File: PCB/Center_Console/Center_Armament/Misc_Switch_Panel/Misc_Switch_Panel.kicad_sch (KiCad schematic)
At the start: 0 parts

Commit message: Misc Switch Panel schematic WIP + gitignore cleanup
- Misc_Switch_Panel: schematic and PCB in-progress (MCP23017, 8-pin JST-XH harness)
- .gitignore: exclude KiCad Fabrication Toolkit outputs (production/, fabrication-toolkit-options.json) and .claude/worktrees/
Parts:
- added J1: Conn_02x04_Top_Bottom, Connector_Molex:Molex_Mini-Fit_Jr_5566-08A_2x04_P4.20mm_Vertical, symbol Connector_Generic:Conn_02x04_Top_Bottom
- added U1: MCP23017x-x-SO, Package_SO:SOIC-28W_7.5x17.9mm_P1.27mm, symbol Interface_Expansion:MCP23017x-x-SO
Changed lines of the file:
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@@
 	(generator_version "10.0")
 	(paper "A4")
+	(symbol
+		(lib_id "Interface_Expansion:MCP23017x-x-SO")
+		(at 68.58 62.23 0)
+		(unit 1)
+		(body_style 1)
+		(exclude_from_sim no)
+		(in_bom yes)
+		(on_board yes)
+		(in_pos_files yes)
+		(dnp no)
+		(fields_autoplaced yes)
+		(property "Reference" "U1"
+			(at 70.7233 34.29 0)
+			(show_name no)
+			(do_not_autoplace no)
+			(effects
+				(font
+					(size 1.27 1.27)
+				)
+				(justify left)
+			)
+		)
+		(property "Value" "MCP23017x-x-SO"
+			(at 70.7233 36.83 0)
+			(show_name no)
+			(do_not_autoplace no)
+			(effects
+				(font
+					(size 1.27 1.27)
+				)
+				(justify left)
+			)
+		)
+		(property "Footprint" "Package_SO:SOIC-28W_7.5x17.9mm_P1.27mm"
+			(at 73.66 87.63 0)
+			(hide yes)
+			(show_name no)
+			(do_not_autoplace no)
+			(effects
+				(font
+					(size 1.27 1.27)
+				)
+				(justify left)
+			)
+		)
+		(property "Datasheet" "https://ww1.microchip.com/downloads/aemDocuments/documents/APID/ProductDocuments/DataSheets/MCP23017-Data-Sheet-DS20001952.pdf"
+			(at 73.66 90.17 0)
+			(hide yes)
+			(show_name no)
+			(do_not_autoplace no)
+			(effects
+				(font
+					(size 1.27 1.27)
+				)
+				(justify left)
+			)
+		)
+		(property "Description" "16-bit I/O expander, I2C, interrupts, w pull-ups, GPA7/GPB7 output only (https://microchip.my.site.com/s/article/GPA7---GPB7-Cannot-Be-Used-as-Inputs-In-MCP23017),  SOIC-28"
+			(at 68.58 62.23 0)
+			(hide yes)
+			(show_name no)
+			(do_not_autoplace no)
+			(effects
+				(font
+					(size 1.27 1.27)
+				)
+			)
+		)
+		(pin "6"
+		)
+		(pin "3"
+		)
+		(pin "1"
+		)
+		(pin "7"
+		)
+		(pin "8"
+		)
+		(pin "2"
+		)
+		(pin "4"
+		)
+		(pin "5"
+		)
+		(pin "9"
+		)
+		(pin "28"
+		)
+		(pin "23"
+		)
+		(pin "26"
+		)
+		(pin "24"
+		)
+		(pin "27"
+		)
+		(pin "25"
+		)
+		(pin "12"
+		)
+		(pin "11"
+		)
+		(pin "10"
+		)
+		(pin "16"
+		)
+		(pin "15"
+		)
+		(pin "17"
+		)
+		(pin "14"
+		)
+		(pin "13"
+		)
+		(pin "22"
+		)
+		(pin "18"
+		)
+		(pin "21"
+		)
+		(pin "20"
+		)
+		(pin "19"
+		)
+		(instances
+			(project "Misc_Switch_Panel"
+				(path "/e216e2c6-0c29-44a6-a74b-9257e68cb7df"
+					(reference "U1")
+					(unit 1)
+				)
+			)
+		)
+	)
+	(symbol
+		(lib_id "Connector_Generic:Conn_02x04_Top_Bottom")
+		(at 140.97 43.18 0)
+		(unit 1)
+		(body_style 1)
+		(exclude_from_sim no)
+		(in_bom yes)
+		(on_board yes)
+		(in_pos_files yes)
+		(dnp no)
+		(fields_autoplaced yes)
+		(property "Reference" "J1"
+			(at 142.24 34.29 0)
+			(show_name no)
+			(do_not_autoplace no)
+			(effects
+				(font
+					(size 1.27 1.27)
+				)
+			)
+		)
+		(property "Value" "Conn_02x04_Top_Bottom"
+			(at 142.24 36.83 0)
+			(show_name no)
+			(do_not_autoplace no)
+			(effects
+				(font
+					(size 1.27 1.27)
+				)
+			)
+		)
+		(property "Footprint" "Connector_Molex:Molex_Mini-Fit_Jr_5566-08A_2x04_P4.20mm_Vertical"
+			(at 140.97 43.18 0)
+			(hide yes)
+			(show_name no)
+			(do_not_autoplace no)
+			(effects
+				(font
+					(size 1.27 1.27)
+				)
+			)
+		)
+		(property "Datasheet" ""
+			(at 140.97 43.18 0)
+			(hide yes)
+			(show_name no)
+			(do_not_autoplace no)
+			(effects
+				(font
+					(size 1.27 1.27)
+				)
+			)
+		)
+		(property "Description" "Generic connector, double row, 02x04, top/bottom pin numbering scheme (row 1: 1...pins_per_row, row2: pins_per_row+1 ... num_pins), script generated (kicad-library-utils/schlib/autogen/connector/)"
+			(at 140.97 43.18 0)
+			(hide yes)
+			(show_name no)
+			(do_not_autoplace no)
+			(effects
+				(font
+					(size 1.27 1.27)
+				)
+			)
+		)
+		(pin "1"
+		)
+		(pin "3"
+		)
+		(pin "2"
+		)
+		(pin "4"
+		)
+		(pin "5"
+		)
+		(pin "6"
+		)
+		(pin "7"
+		)
+		(pin "8"
+		)
+		(instances
+			(project "Misc_Switch_Panel"
+				(path "/e216e2c6-0c29-44a6-a74b-9257e68cb7df"
+					(reference "J1")
+					(unit 1)
+				)
+			)
+		)
+	)
 	(sheet_instances
 		(path "/"

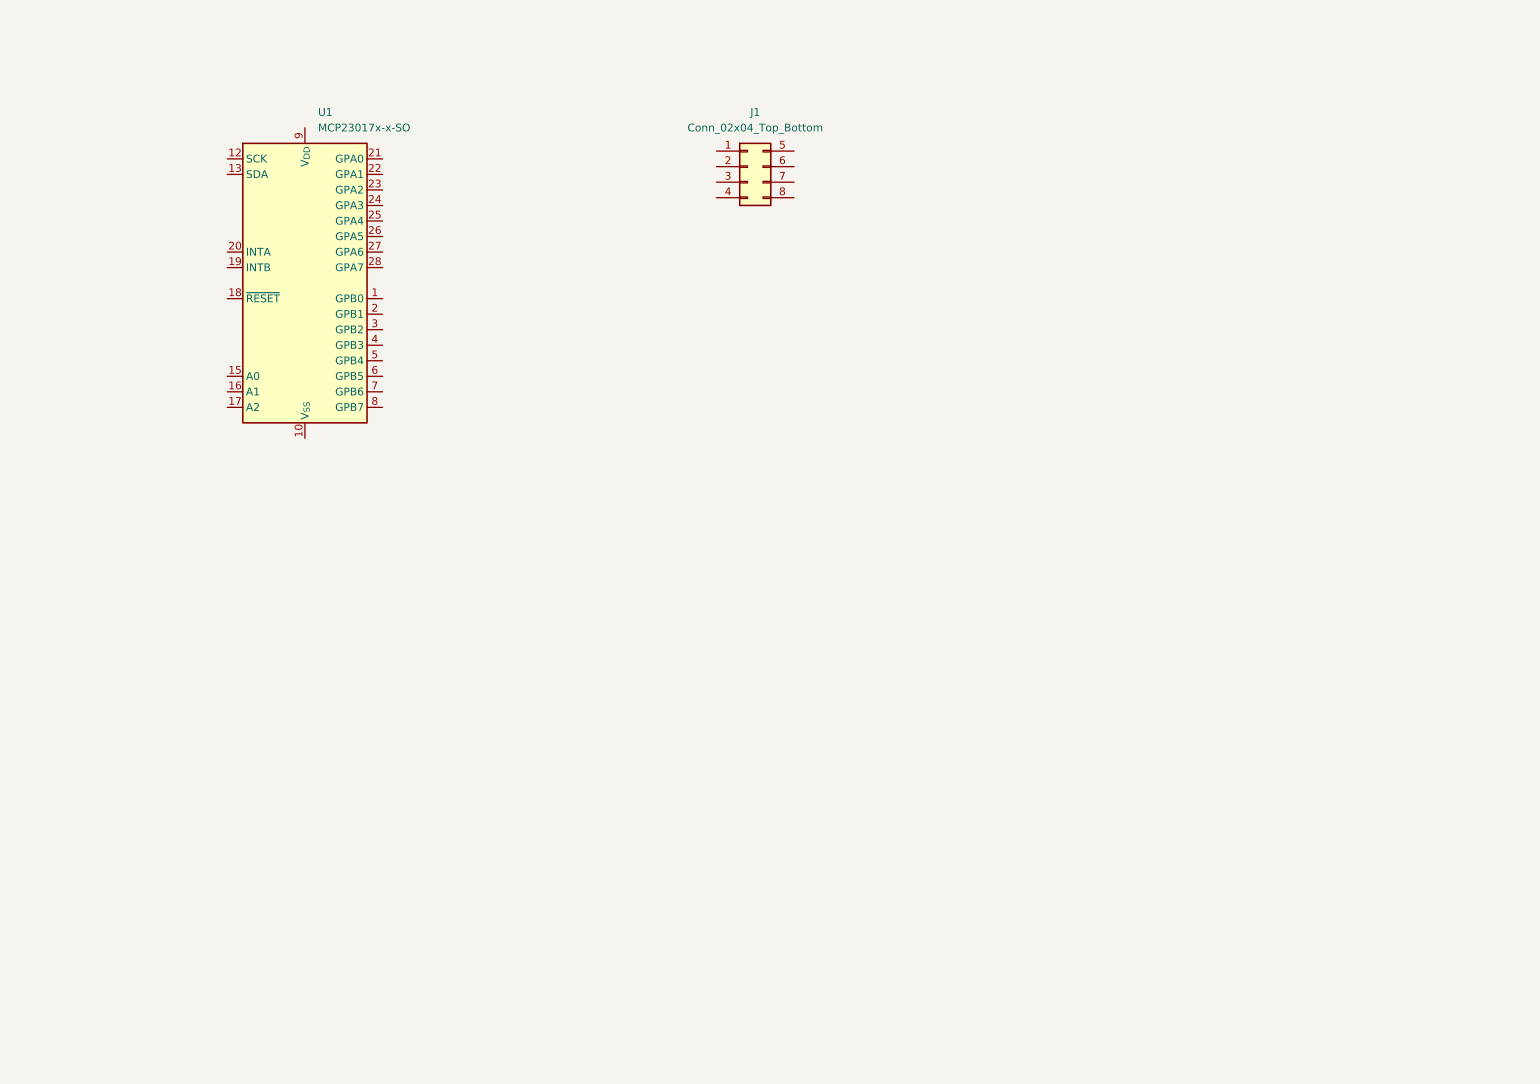
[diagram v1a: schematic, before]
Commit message: Complete Misc Switch Panel schematic and establish shared PCB infrastructure
Misc Switch Panel schematic (3 sheets, 0 ERC violations):
- Controls sheet: MCP23017 @ 0x22, 8-pin JST-XH harness (J1), address/reset
  resistors, I2C series (33Ω) and interrupt protection (100Ω) resistors
- Switches sheet: J2/J3 8-pin JST-XH connectors, all panel-mounted switch and
  pot symbols (exclude_from_board)
- Backlighting sheet: 3× 5-LED series strings, 120Ω per string, hierarchical
  labels +12V_BACKLIGHT / BACKLIGHT_SW_RETURN
- LED zone switching: IRLML2502 N-ch low-side MOSFET, gate driven directly by
  STM32 3.3V PWM; LED power on separate 2-pin Mini-Fit Jr (J4), not on signal
  harness — eliminates NPN+zener gate driver complexity

Shared KiCad project infrastructure:
- /new-kicad-project skill: scaffolds directory, lib tables, .kicad_pro, and
  minimal root .kicad_sch in one step; tailored next-steps for mcu vs breakout
- PCB/Libraries/project-template/template.kicad_pro: JLCPCB design rules,
  predefined track widths (0.2/0.3/0.5/1.0mm), via sizes (0.3/0.6, 0.4/0.8mm),
  4 net classes (Default, LED_Trunk, LED_String, CAN), silkscreen defaults
- PCB/Libraries/design-rules/jlcpcb-standard.kicad_dru: custom DRC rules for
  copper-to-edge, silkscreen width, hole-to-hole, CAN diff pair
- PCB/Libraries/sheets/README.md: shared hierarchical sheet template library
  (placeholder; templates added as standard blocks are completed)
- Misc_Switch_Panel.kicad_pro patched with all of the above

PCB design rules documented (Docs/claude/pcb-design-rules.md):
- JLCPCB standard 2-layer constraints; min trace/clearance bumped to 0.2mm
  (floor matches Default class — all DRC violations are meaningful)
- Net class table with sizing rationale; power classes deferred pending actuator
  board architecture; 500mA per-board limit for logic+LED boards established
- Actuator board checklist placeholder (solenoids, servos, large steppers)
- JLCPCB cost-optimised ordering settings from bench-verified s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
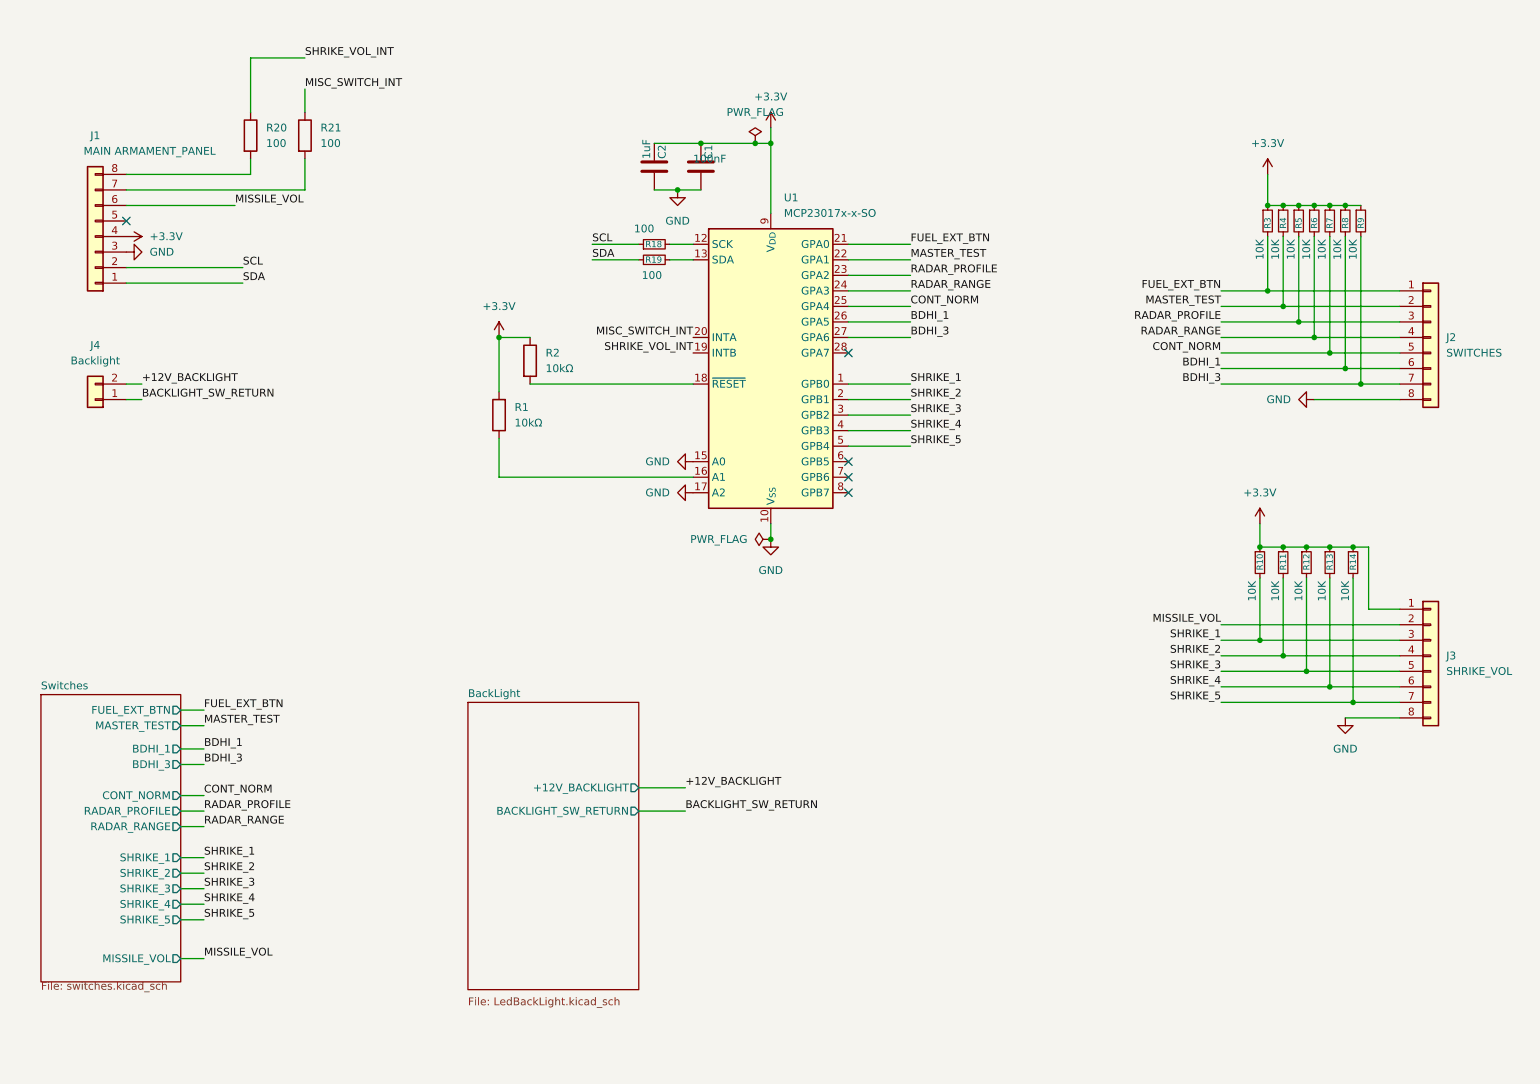
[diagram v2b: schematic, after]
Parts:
- removed J1: Conn_02x04_Top_Bottom, Connector_Molex:Molex_Mini-Fit_Jr_5566-08A_2x04_P4.20mm_Vertical, symbol Connector_Generic:Conn_02x04_Top_Bottom
- added C1: 100nF, Capacitor_SMD:C_0805_2012Metric, symbol Device:C
- added C2: 1uF, Capacitor_SMD:C_0805_2012Metric, symbol Device:C
- added J1: MAIN ARMAMENT_PANEL, Connector_JST:JST_XH_B8B-XH-A_1x08_P2.50mm_Vertical, symbol Connector_Generic:Conn_01x08
- added J2: SWITCHES, Connector_JST:JST_XH_B8B-XH-A_1x08_P2.50mm_Vertical, symbol Connector_Generic:Conn_01x08
- added J3: SHRIKE_VOL, Connector_JST:JST_XH_B8B-XH-A_1x08_P2.50mm_Vertical, symbol Connector_Generic:Conn_01x08
- added J4: Backlight, Connector_Molex:Molex_Mini-Fit_Jr_5566-02A_2x01_P4.20mm_Vertical, symbol Connector_Generic:Conn_01x02
- added R1, R2: 10kΩ, Resistor_SMD:R_1206_3216Metric, symbol Device:R
- added R10, R11, R12, R13, R14, R3, R4, R5, R6, R7, R8, R9: 10K, Resistor_SMD:R_0805_2012Metric, symbol Device:R_Small
- added R18, R19: 100, Resistor_SMD:R_0805_2012Metric, symbol Device:R_Small
- added R20, R21: 100, Resistor_SMD:R_1206_3216Metric, symbol Device:R
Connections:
- net SHRIKE_1: now reaches U1.1 (GPB0)
- net SHRIKE_1: now also J3.3 (Pin_3), R10.2
- net GND: now reaches U1.10 (V_{SS})
- net GND: now also U1.15 (A0), U1.17 (A2), C1.2, C2.2, J1.3 (Pin_3), J2.8 (Pin_8), J3.8 (Pin_8)
- net at U1.12 (SCK): now also R18.2
- net at U1.13 (SDA): now also R19.2
- net at U1.16 (A1): now also R1.1
- net at U1.18 (~{RESET}): now also R2.2
- net SHRIKE_VOL_INT: now reaches U1.19 (INTB)
- net SHRIKE_VOL_INT: now also R20.1
- net SHRIKE_2: now reaches U1.2 (GPB1)
- net SHRIKE_2: now also J3.4 (Pin_4), R11.2
- net MISC_SWITCH_INT: now reaches U1.20 (INTA)
- net MISC_SWITCH_INT: now also R21.1
- net FUEL_EXT_BTN: now reaches U1.21 (GPA0)
- net FUEL_EXT_BTN: now also J2.1 (Pin_1), R3.2
- net MASTER_TEST: now reaches U1.22 (GPA1)
- net MASTER_TEST: now also J2.2 (Pin_2), R4.2
- net RADAR_PROFILE: now reaches U1.23 (GPA2)
- net RADAR_PROFILE: now also J2.3 (Pin_3), R5.2
- net RADAR_RANGE: now reaches U1.24 (GPA3)
- net RADAR_RANGE: now also J2.4 (Pin_4), R6.2
- net CONT_NORM: now reaches U1.25 (GPA4)
- net CONT_NORM: now also J2.5 (Pin_5), R7.2
- net BDHI_1: now reaches U1.26 (GPA5)
- net BDHI_1: now also J2.6 (Pin_6), R8.2
- net BDHI_3: now reaches U1.27 (GPA6)
- net BDHI_3: now also J2.7 (Pin_7), R9.2
- net SHRIKE_3: now reaches U1.3 (GPB2)
- net SHRIKE_3: now also J3.5 (Pin_5), R12.2
- net SHRIKE_4: now reaches U1.4 (GPB3)
- net SHRIKE_4: now also J3.6 (Pin_6), R13.2
- net SHRIKE_5: now reaches U1.5 (GPB4)
- net SHRIKE_5: now also J3.7 (Pin_7), R14.2
- net +3.3V: now reaches U1.9 (V_{DD})
- net +3.3V: now also C1.1, C2.1, J1.4 (Pin_4), J3.1 (Pin_1), R1.2, R10.1, R11.1, R12.1, R13.1, R14.1, R2.1, R3.1, R4.1, R5.1, R6.1, R7.1, R8.1, R9.1
- new net: J1.7 (Pin_7), R21.2
- new net: J1.8 (Pin_8), R20.2
- new net +12V_BACKLIGHT: J4.2 (Pin_2)
- new net BACKLIGHT_SW_RETURN: J4.1 (Pin_1)
- new net MISSILE_VOL: J1.6 (Pin_6), J3.2 (Pin_2)
- new net SCL: J1.2 (Pin_2), R18.1
- new net SDA: J1.1 (Pin_1), R19.1
- no-connect marks 0 -> 5
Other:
- added sheet BackLight (LedBackLight.kicad_sch)
- added sheet Switches (switches.kicad_sch)
- moved on the sheet: U1

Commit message: Fix LED_5050_Red symbol polarity: K=pin1, A=pin2
Symbol body was mirrored vs standard Device:LED convention — pin 1 was
labelled A and pin 2 K. Flipped triangle/bar to point left and swapped
pin names so K=1 (left) and A=2 (right), matching the generic KiCad LED
symbol.

Physical LED verified: notched/chamfered corner is the ANODE. Footprint
pad positions unchanged — pad2 (left, where the silkscreen marker sits)
is now correctly the anode. Updated kicad.md to document this.

Also includes Misc_Switch_Panel schematic edits from current KiCad session.
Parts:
- added D1, D2: LED, LED_SMD:LED_0805_2012Metric, symbol Device:LED
- added R22: R, Resistor_SMD:R_0805_2012Metric, symbol Device:R
- added R23: R, Capacitor_SMD:C_0805_2012Metric, symbol Device:R
- C1: value 100nF -> C
- C2: value 1uF -> C
- J1: value MAIN ARMAMENT_PANEL -> Conn_01x08
- J2: value SWITCHES -> Conn_01x08
- J3: value SHRIKE_VOL -> Conn_01x08
- J4: value Backlight -> Conn_01x02
- R1, R2: value 10kΩ -> R
- R10, R11, R12, R13, R14, R3, R4, R5, R6, R7, R8, R9: value 10K -> R_Small
- R18, R19: value 100 -> R_Small
- R20, R21: value 100 -> R; footprint Resistor_SMD:R_1206_3216Metric -> Resistor_SMD:R_0805_2012Metric
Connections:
- net +12V_BACKLIGHT: now also R23.1
- net +3.3V: now also R22.1
- net BACKLIGHT_SW_RETURN: now also D2.1 (K)
- net GND: now also D1.1 (K)
- new net: D2.2 (A), R23.2
- new net: D1.2 (A), R22.2
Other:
- note added: "Status LED Indicators"
- moved on the sheet: J1, J4, R20, R21

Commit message: Scaffold AWRS_Panel and Armament_MCU KiCad projects
- AWRS_Panel: breakout board scaffold (sym-lib-table, fp-lib-table,
  jlcpcb-standard.kicad_dru, .kicad_pro, .kicad_sch)
- Armament_MCU: MCU board scaffold (same set of files)
- Add controller stub docs: AWRS_Panel.md and Armament_Panel.md
- Update Center_Armament.md harness section: J1→AWRS_Panel and
  J2→Misc_Switch_Panel documented as two distinct connectors with
  full pinouts; J2_LED Mini-Fit Jr added
- Misc_Switch_Panel: KiCad reformatted files on project open
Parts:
- C1: value C -> 100nF
- C2: value C -> 1uF
- D1: value LED -> POWER_ST
- D2: value LED -> BACKLIGHT_ST
- J1: value Conn_01x08 -> MAIN_ARMAMENT_PANEL
- J2: value Conn_01x08 -> SWITCHES
- J3: value Conn_01x08 -> SHRIKE_VOL
- J4: value Conn_01x02 -> LED_BACKLIGHT
- R1, R2: value R -> 10k
- R10, R11, R12, R13, R14, R3, R4, R5, R6, R7, R8, R9: value R_Small -> 10k
- R18, R19: value R_Small -> 100
- R20, R21: value R -> 100
- R22: value R -> 3.3k
- R23: value R -> 22k
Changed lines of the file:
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@@
 			)
 		)
-		(property "Value" "R_Small"
+		(property "Value" "10k"
 			(at 234.95 58.42 90)
 			(show_name no)
@@
 			)
 		)
-		(property "Value" "R_Small"
+		(property "Value" "100"
 			(at 127 60.96 90)
 			(show_name no)
@@
 			)
 		)
-		(property "Value" "Conn_01x08"
+		(property "Value" "MAIN_ARMAMENT_PANEL"
 			(at 38.1 35.56 0)
 			(show_name no)
@@
 			)
 		)
-		(property "Value" "R_Small"
+		(property "Value" "10k"
 			(at 234.95 114.3 90)
 			(show_name no)
@@
 			)
 		)
-		(property "Value" "R_Small"
+		(property "Value" "100"
 			(at 125.73 53.34 90)
 			(show_name no)
@@
 			)
 		)
-		(property "Value" "Conn_01x08"
+		(property "Value" "SHRIKE_VOL"
 			(at 255.27 125.7299 0)
 			(show_name no)
@@
 			)
 		)
-		(property "Value" "R_Small"
+		(property "Value" "10k"
 			(at 240.03 58.42 90)
 			(show_name no)
@@
 			)
 		)
-		(property "Value" "LED"
+		(property "Value" "BACKLIGHT_ST"
 			(at 41.91 102.87 0)
 			(show_name no)
@@
 			)
 		)
-		(property "Value" "R_Small"
+		(property "Value" "10k"
 			(at 227.33 58.42 90)
 			(show_name no)
@@
 			)
 		)
-		(property "Value" "R"
+		(property "Value" "100"
 			(at 66.04 34.2899 0)
 			(show_name no)
@@
 			)
 		)
-		(property "Value" "LED"
+		(property "Value" "POWER_ST"
 			(at 27.94 102.87 0)
 			(show_name no)
@@
 			)
 		)
-		(property "Value" "R"
+		(property "Value" "10k"
 			(at 102.87 85.0899 0)
 			(show_name no)
@@
 			)
 		)
-		(property "Value" "R_Small"
+		(property "Value" "10k"
 			(at 231.14 114.3 90)
 			(show_name no)
@@
 			)
 		)
-		(property "Value" "R_Small"
+		(property "Value" "10k"
 			(at 229.87 58.42 90)
 			(show_name no)
@@
 			)
 		)
-		(property "Value" "Conn_01x08"
+		(property "Value" "SWITCHES"
 			(at 255.27 73.6599 0)
 			(show_name no)
@@
 			)
 		)
-		(property "Value" "R_Small"
+		(property "Value" "10k"
 			(at 237.49 58.42 90)
 			(show_name no)
@@
 			)
 		)
-		(property "Value" "R_Small"
+		(property "Value" "10k"
 			(at 238.76 114.3 90)
 			(show_name no)
@@
 			)
 		)
-		(property "Value" "C"
+		(property "Value" "1uF"
 			(at 124.46 41.91 90)
 			(show_name no)
@@
 			)
 		)
-		(property "Value" "R"
+		(property "Value" "10k"
 			(at 107.95 76.1999 0)
 			(show_name no)
@@
 			)
 		)
-		(property "Value" "R_Small"
+		(property "Value" "10k"
 			(at 227.33 114.3 90)
 			(show_name no)
@@
 			)
 		)
-		(property "Value" "Conn_01x02"
+		(property "Value" "LED_BACKLIGHT"
 			(at 29.21 69.85 0)
 			(show_name no)
@@
 			)
 		)
-		(property "Value" "C"
+		(property "Value" "100nF"
 			(at 132.08 41.91 0)
 			(show_name no)
@@
 			)
 		)
-		(property "Value" "R"
+		(property "Value" "22k"
 			(at 46.99 101.6 90)
 			(show_name no)
@@
 			)
 		)
-		(property "Value" "R"
+		(property "Value" "3.3k"
 			(at 33.02 101.6 90)
 			(show_name no)
@@
 			)
 		)
-		(property "Value" "R_Small"
+		(property "Value" "10k"
 			(at 223.52 114.3 90)
 			(show_name no)
@@
 			)
 		)
-		(property "Value" "R_Small"
+		(property "Value" "10k"
 			(at 224.79 58.42 90)
 			(show_name no)
@@
 			)
 		)
-		(property "Value" "R_Small"
+		(property "Value" "10k"
 			(at 232.41 58.42 90)
 			(show_name no)
@@
 			)
 		)
-		(property "Value" "R"
+		(property "Value" "100"
 			(at 57.15 34.2899 0)
 			(show_name no)
